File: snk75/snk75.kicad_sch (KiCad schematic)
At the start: 19 parts, among them J1 AVR-ISP-6, J2 TYPE-C-31-M12_13, U1 ATmega32U4-AU, U2 USBLC6-2SC6, Y1 16MHZ

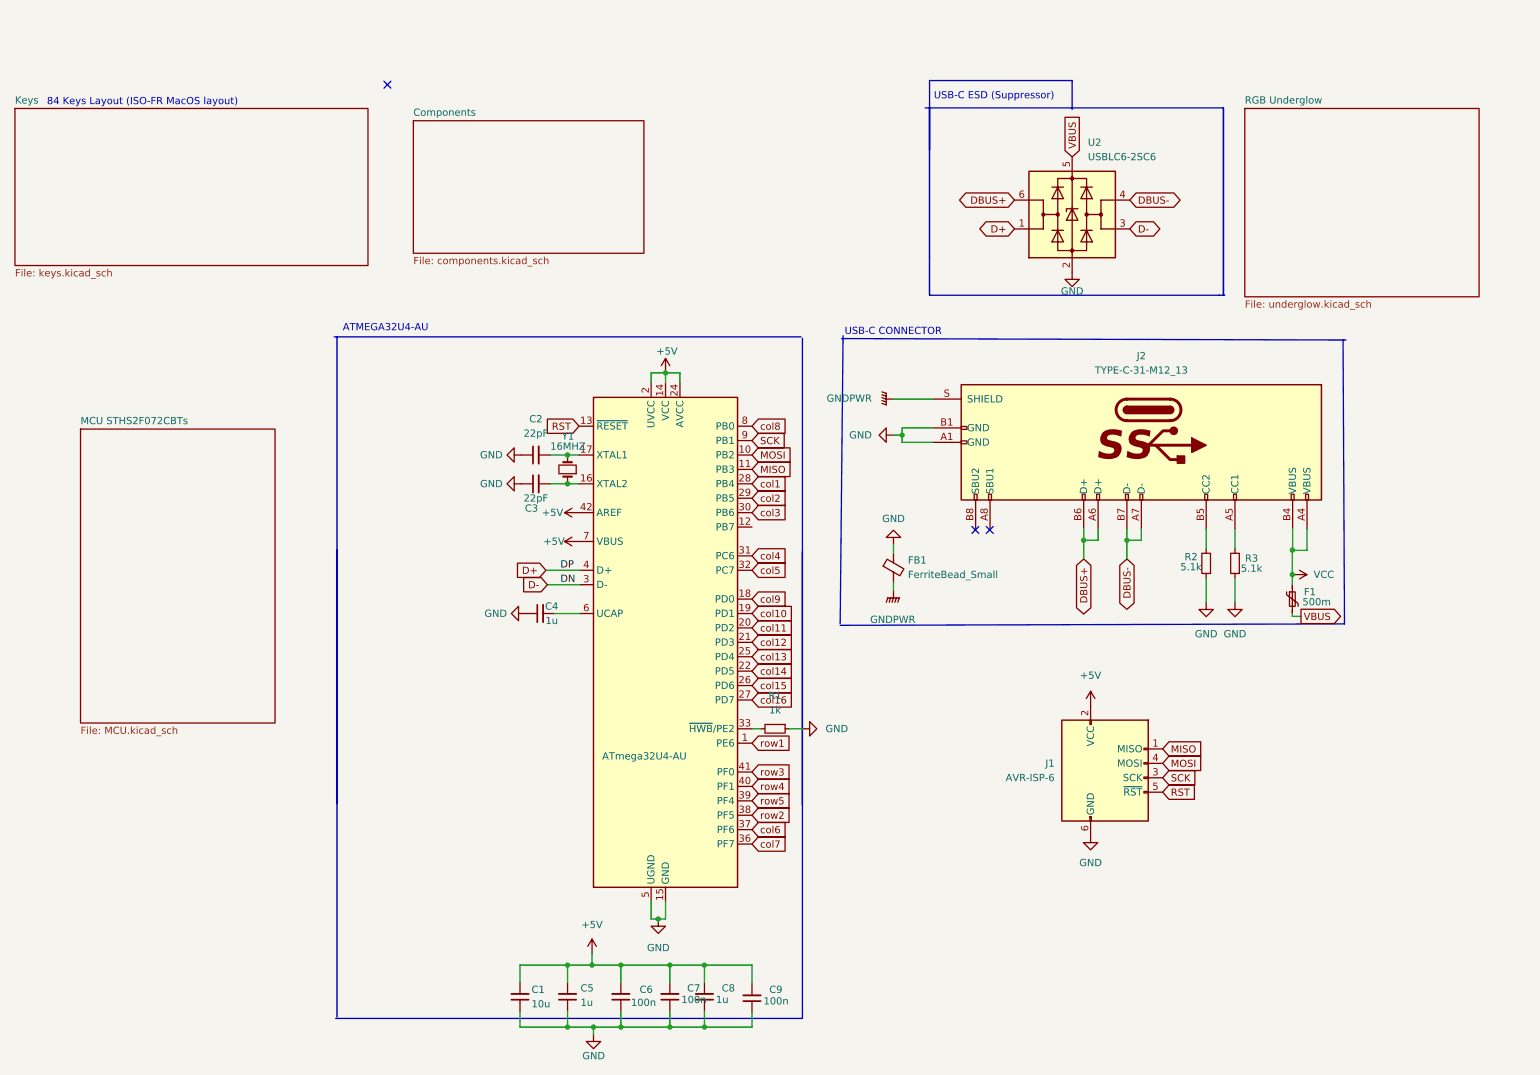
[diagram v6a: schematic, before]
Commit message: added new row layout and connected row1 to MCU
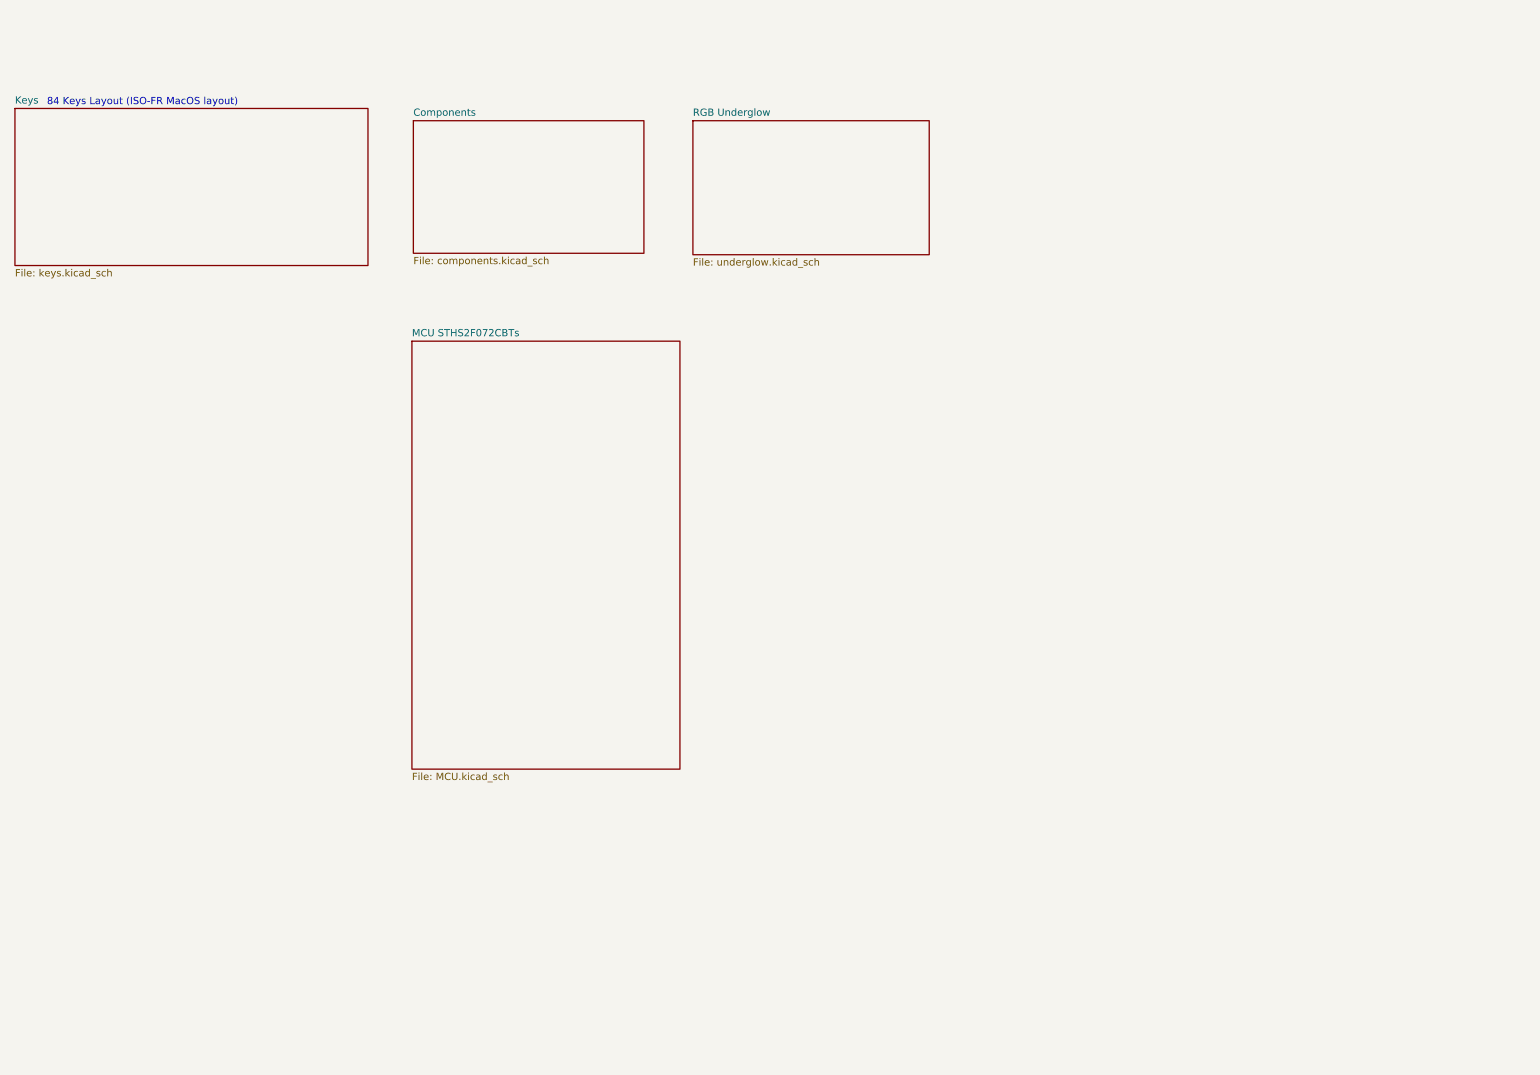
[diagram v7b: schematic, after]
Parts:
- removed C1: 10u, Capacitor_SMD:C_0402_1005Metric, symbol Device:C_Small
- removed C2: 22pF, Capacitor_SMD:C_0402_1005Metric, symbol Device:C_Small
- removed C3: 22pF, Capacitor_SMD:C_0402_1005Metric_Pad0.74x0.62mm_HandSolder, symbol Device:C_Small
- removed C4: 1u, Capacitor_SMD:C_0402_1005Metric_Pad0.74x0.62mm_HandSolder, symbol Device:C_Small
- removed C5, C8: 1u, Capacitor_SMD:C_0402_1005Metric, symbol Device:C_Small
- removed C6, C7, C9: 100n, Capacitor_SMD:C_0402_1005Metric, symbol Device:C_Small
- removed F1: 500m, symbol Device:Polyfuse_Small
- removed FB1: FerriteBead_Small, Inductor_SMD:L_0805_2012Metric, symbol Device:FerriteBead_Small
- removed J1: AVR-ISP-6, symbol Connector:AVR-ISP-6
- removed J2: TYPE-C-31-M12_13, acheron_Connectors:TYPE-C-31-M-12, symbol acheronSymbols:TYPE-C-31-M12_13
- removed R1: 1k, Resistor_SMD:R_0402_1005Metric, symbol Device:R_Small
- removed R2, R3: 5.1k, Resistor_SMD:R_0402_1005Metric, symbol Device:R_Small
- removed U1: ATmega32U4-AU, Package_QFP:TQFP-44_10x10mm_P0.8mm, symbol MCU_Microchip_ATmega:ATmega32U4-A
- removed U2: USBLC6-2SC6, acheron_Components:SOT-23-6, symbol Power_Protection:USBLC6-2SC6
- removed Y1: 16MHZ, Crystal:Crystal_SMD_5032-2Pin_5.0x3.2mm_HandSoldering, symbol Device:Crystal_Small
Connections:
- no-connect marks 3 -> 0
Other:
- note removed: "ATMEGA32U4-AU"
- note removed: "USB-C CONNECTOR"
- note removed: "USB-C ESD (Suppressor)"
